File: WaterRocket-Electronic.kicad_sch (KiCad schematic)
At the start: 9 parts, among them J1 Screw_Terminal_01x02, SW1 SW_SPDT, U1 MPU_6050

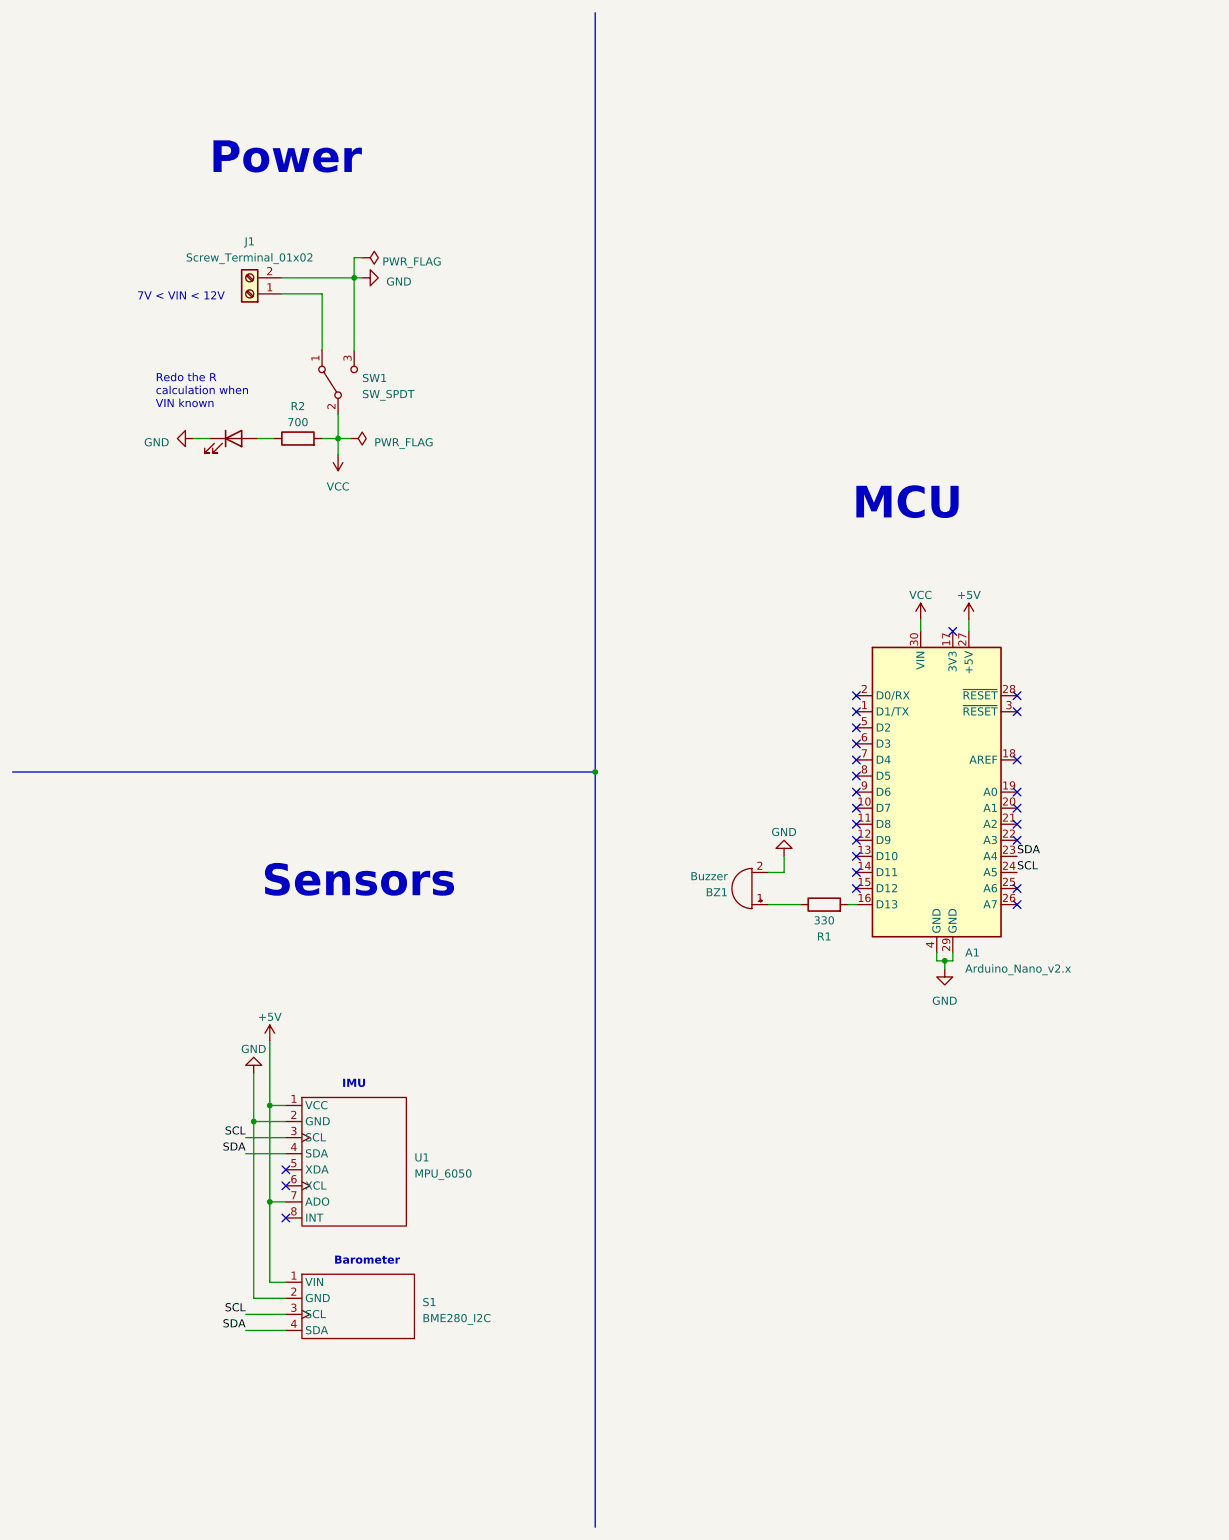
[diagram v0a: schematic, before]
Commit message: Added servomotor, exported
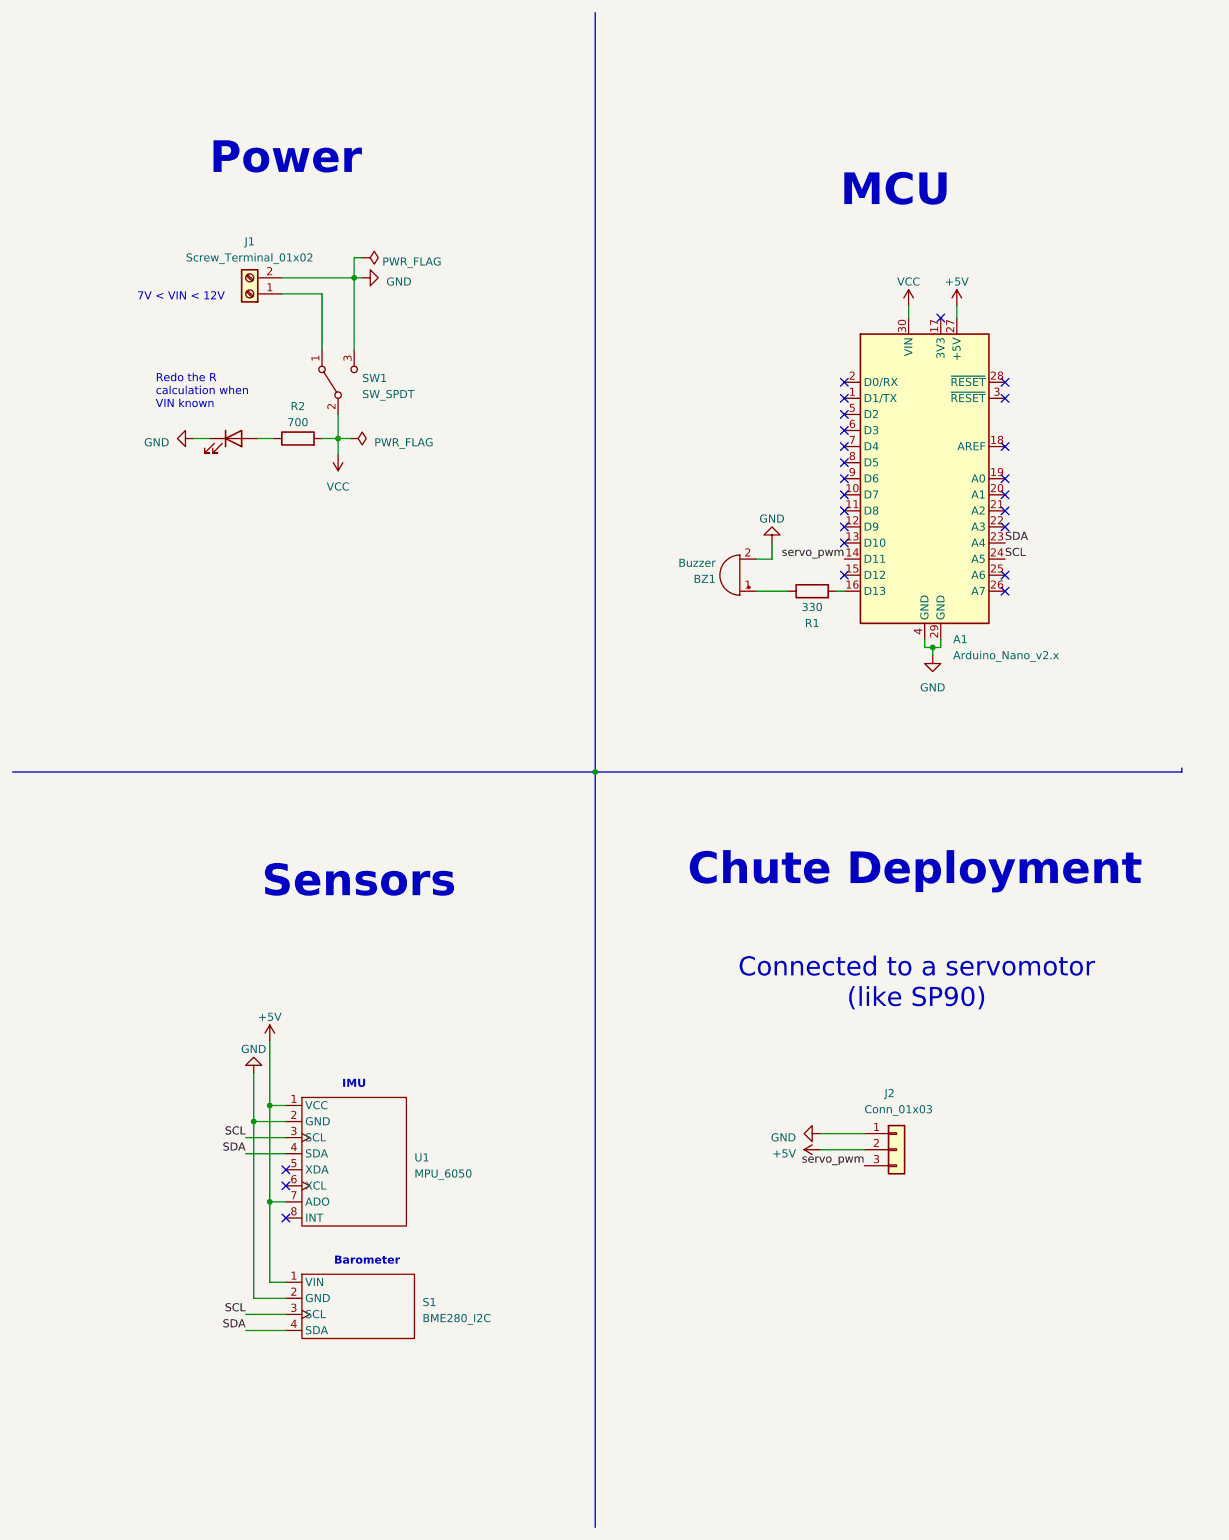
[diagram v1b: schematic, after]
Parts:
- added J2: Conn_01x03, Connector_PinHeader_2.54mm:PinHeader_1x03_P2.54mm_Vertical, symbol Connector_Generic:Conn_01x03
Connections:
- net +5V: now also J2.2 (Pin_2)
- net GND: now also J2.1 (Pin_1)
- net servo_pwm: now reaches A1.14 (D11)
- net servo_pwm: now also J2.3 (Pin_3)
- no-connect marks 26 -> 25
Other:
- note added: "Chute Deployment"
- title: WaterRocket Electronic -> WaterRocket Avionic
- moved on the sheet: A1, BZ1, R1
